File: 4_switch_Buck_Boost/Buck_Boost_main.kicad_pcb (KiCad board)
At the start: 4 copper layers, 95 parts, among them J1 Conn_02x02_Counter_Clockwise, J2 Screw_Terminal_2x5.08, J3 Screw_Terminal_2x2.54, J4 Screw_Terminal_2x5.08, Q1 CSD18532Q5B, Q101 2N7002K, Q102 NVMFS6H836NLT1G, Q103 BSS83P, Q2 CSD18532Q5B, Q3 CSD18532Q5B, Q4 CSD18532Q5B, U1 LT8390EUFD_PBF, U101 LTC4372CMS8-PBF

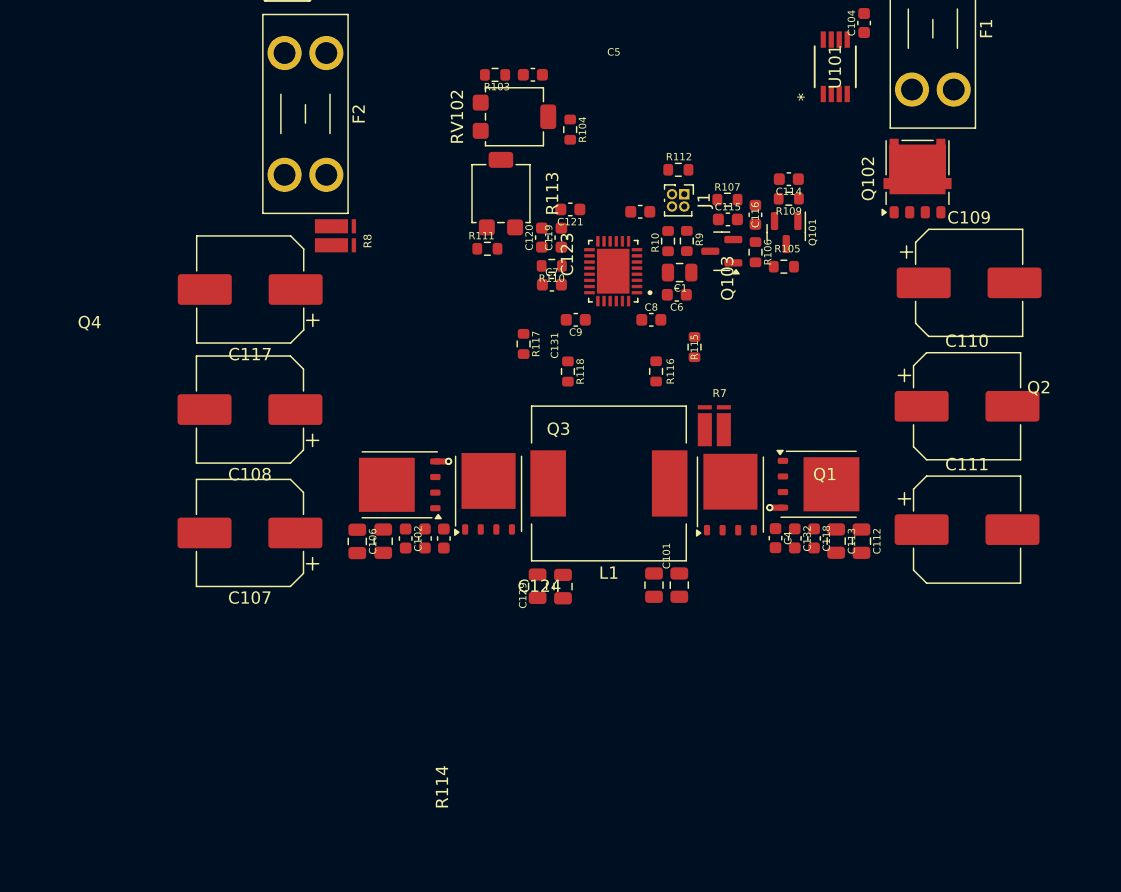
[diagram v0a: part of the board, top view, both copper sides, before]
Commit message: Latest FET and Inductor update, Connected Analog traces
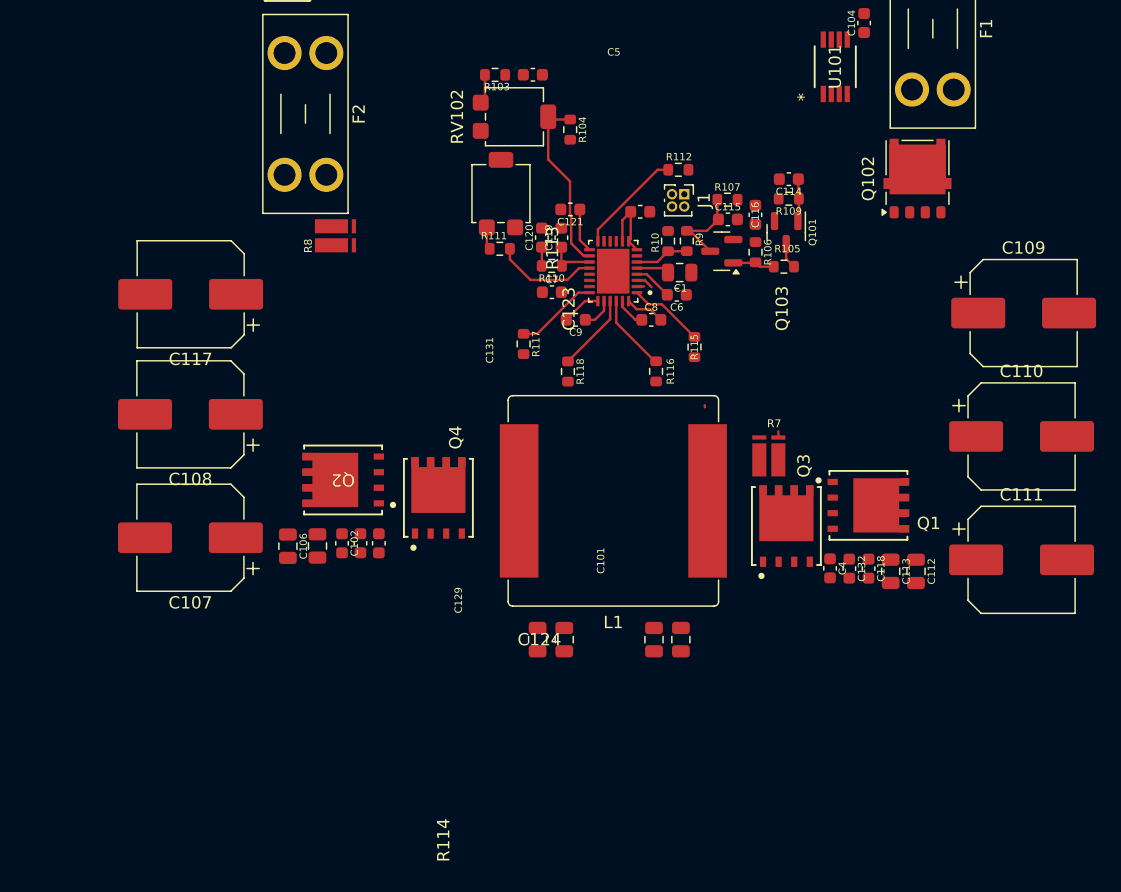
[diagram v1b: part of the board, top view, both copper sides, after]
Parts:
- L1: footprint Inductor_SMD:L_Wuerth_WE-PD-Typ-LS -> Inductor_SMD:L_Bourns_SRP1770TA_16.9x16.9mm
- Q1, Q2, Q3, Q4: value CSD18532Q5B -> BSC070N10LS5ATMA1; footprint Package_TO_SOT_SMD:TDSON-8-1 -> Infineon BSC070:PG-TDSON-8-7_INF
- moved C106 5.66 mm to (117.7, 124.2)
- moved C101 5.37 mm to (120.2, 124.2)
- moved C131 5.31 mm to (125.2, 124.0)
- moved C129 5.27 mm to (123.7, 124.0)
- moved Q3 5.23 mm to (158.3, 122.5)
- moved C102 5.20 mm to (122.2, 124.0)
- moved C109 5.08 mm to (177.7, 105.2)
- moved C4 5.08 mm to (161.9, 126.0)
- moved C110 5.08 mm to (177.5, 115.2)
- moved C111 5.08 mm to (177.5, 125.3)
- moved C112 5.08 mm to (168.9, 126.2)
- moved C113 5.08 mm to (166.8, 126.2)
- moved C118 5.08 mm to (165.0, 126.0)
- moved C132 5.08 mm to (163.5, 126.0)
- moved R7 5.08 mm to (156.9, 116.8)
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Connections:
- C124 pad 1: SW2 -> Net-(C124-Pad1)
- C124 pad 2: Net-(C124-Pad2) -> SW2
- R113 pad 1: Net-(C123-Pad2) -> GND
- R113 pad 2: GND -> Net-(C123-Pad2)
- R114 pad 1: Net-(C124-Pad2) -> GND
- R114 pad 2: GND -> Net-(C124-Pad1)
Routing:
- net FB: track 0.00 -> 14.9 mm
- net Net-(U1-~{PGOOD}): track 0.00 -> 8.70 mm
- net Net-(U1-RT): track 0.00 -> 8.43 mm
- net Net-(Q103-D): track 0.00 -> 7.20 mm
- net TG2_CTRL: track 0.00 -> 6.75 mm
- net BG2_CTRL: track 0.00 -> 6.33 mm
- net BG1_CTRL: track 0.00 -> 6.30 mm
- net TG1_CTRL: track 0.00 -> 6.18 mm
- net /Vref: track 0.00 -> 6.13 mm
- net EN/UVLO: track 0.00 -> 4.43 mm
- net Net-(U1-VC): track 0.00 -> 3.92 mm
- net Net-(U1-SS): track 0.00 -> 3.61 mm
- net ENABLE: track 0.00 -> 3.47 mm
- net Net-(Q103-G): track 0.00 -> 3.46 mm
- net SW1: track 0.00 -> 3.26 mm
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
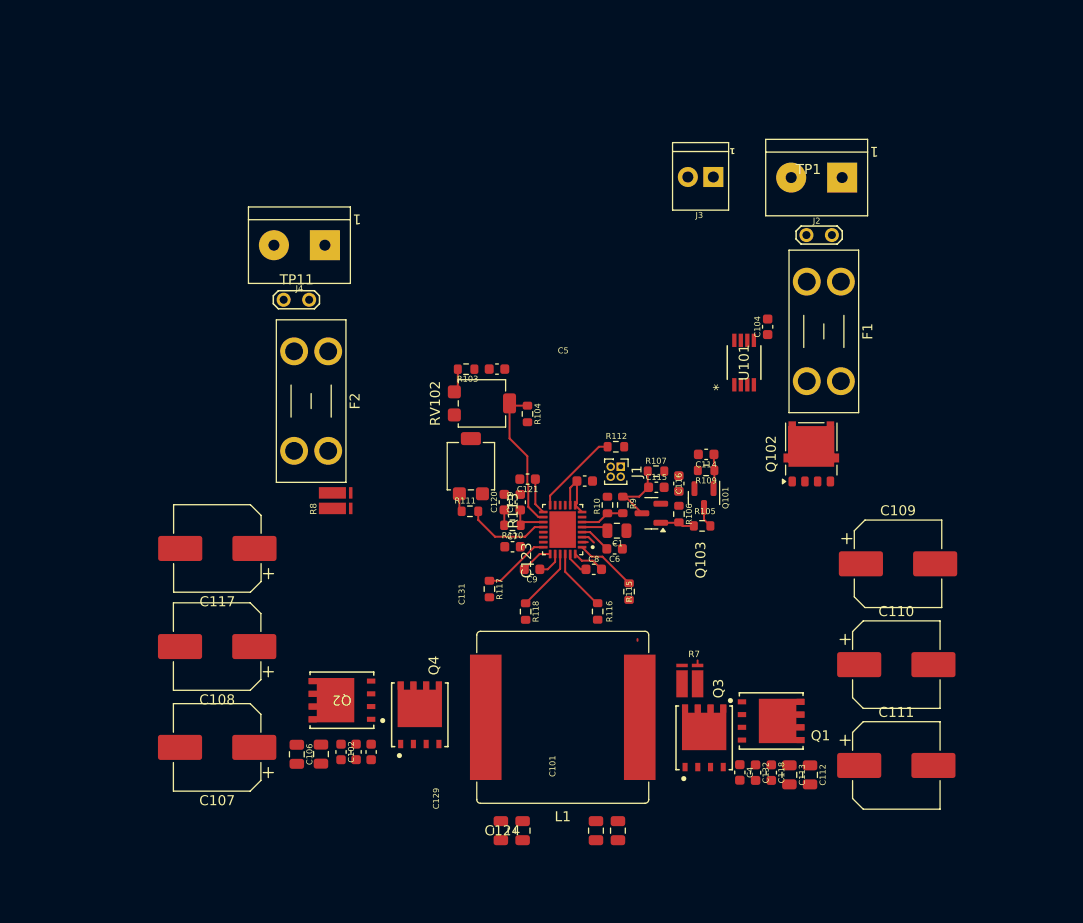
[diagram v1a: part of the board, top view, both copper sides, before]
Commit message: All 4 layers configured
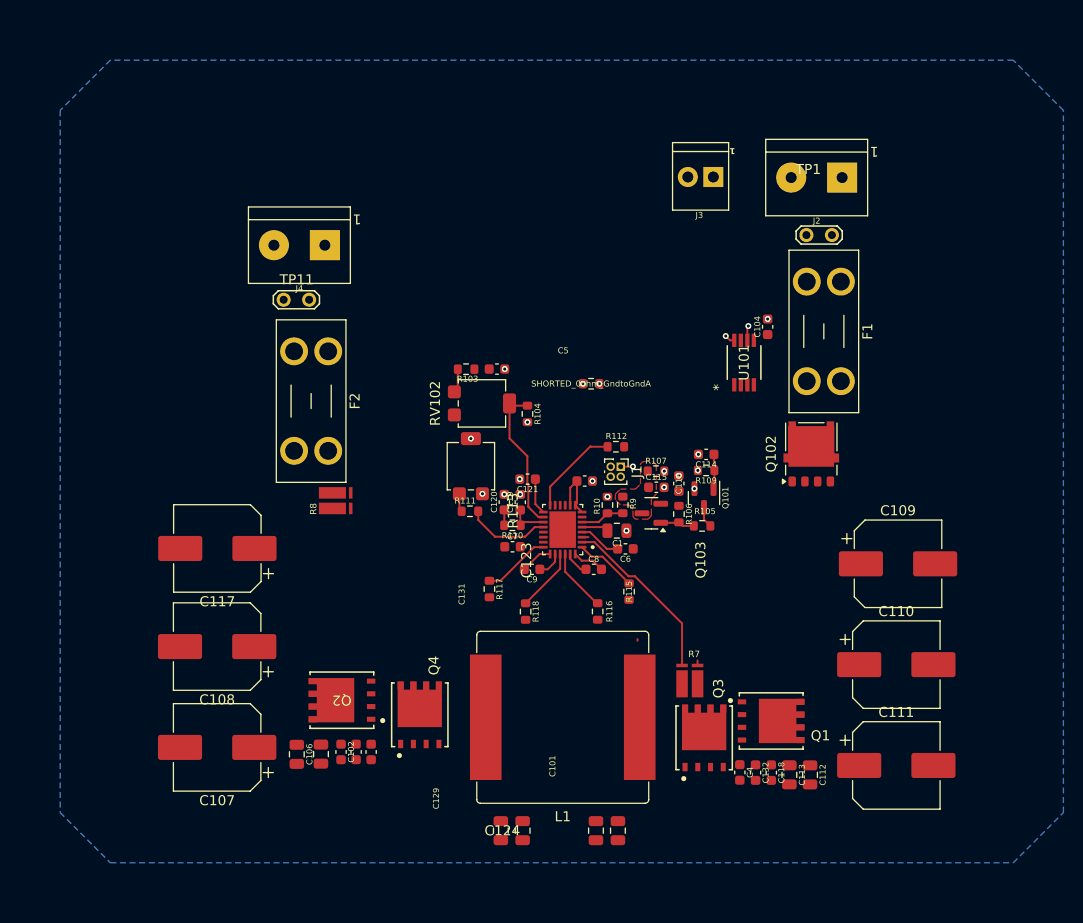
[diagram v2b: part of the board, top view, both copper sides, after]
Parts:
- added SHORTED_0ohm_GndtoGndA: R_short, rsx_resistors:R_0603_1608Metric, F.Cu at (147.1, 87.2)
- moved C6 1.08 mm to (150.5, 103.7)
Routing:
- net LSP: track 0.75 -> 17.7 mm
- net Net-(Q103-D): track 7.20 -> 0.37 mm
- net GND: track 0.00 -> 2.49 mm, vias 0 -> 10
- net GNDA: track 0.00 -> 1.23 mm, vias 0 -> 12
- net Vin: track 3.66 -> 4.74 mm
- net LSN: track 1.92 -> 1.14 mm
- net Net-(U1-~{PGOOD}): track 8.70 -> 9.25 mm
- added copper zone on B.Cu, net GND
- added copper zone on In1.Cu, net GND
- added copper zone on In1.Cu, net GNDA
- added copper zone on F.Cu, net Net-(Q103-D)
- added copper zone on In2.Cu, net Vin

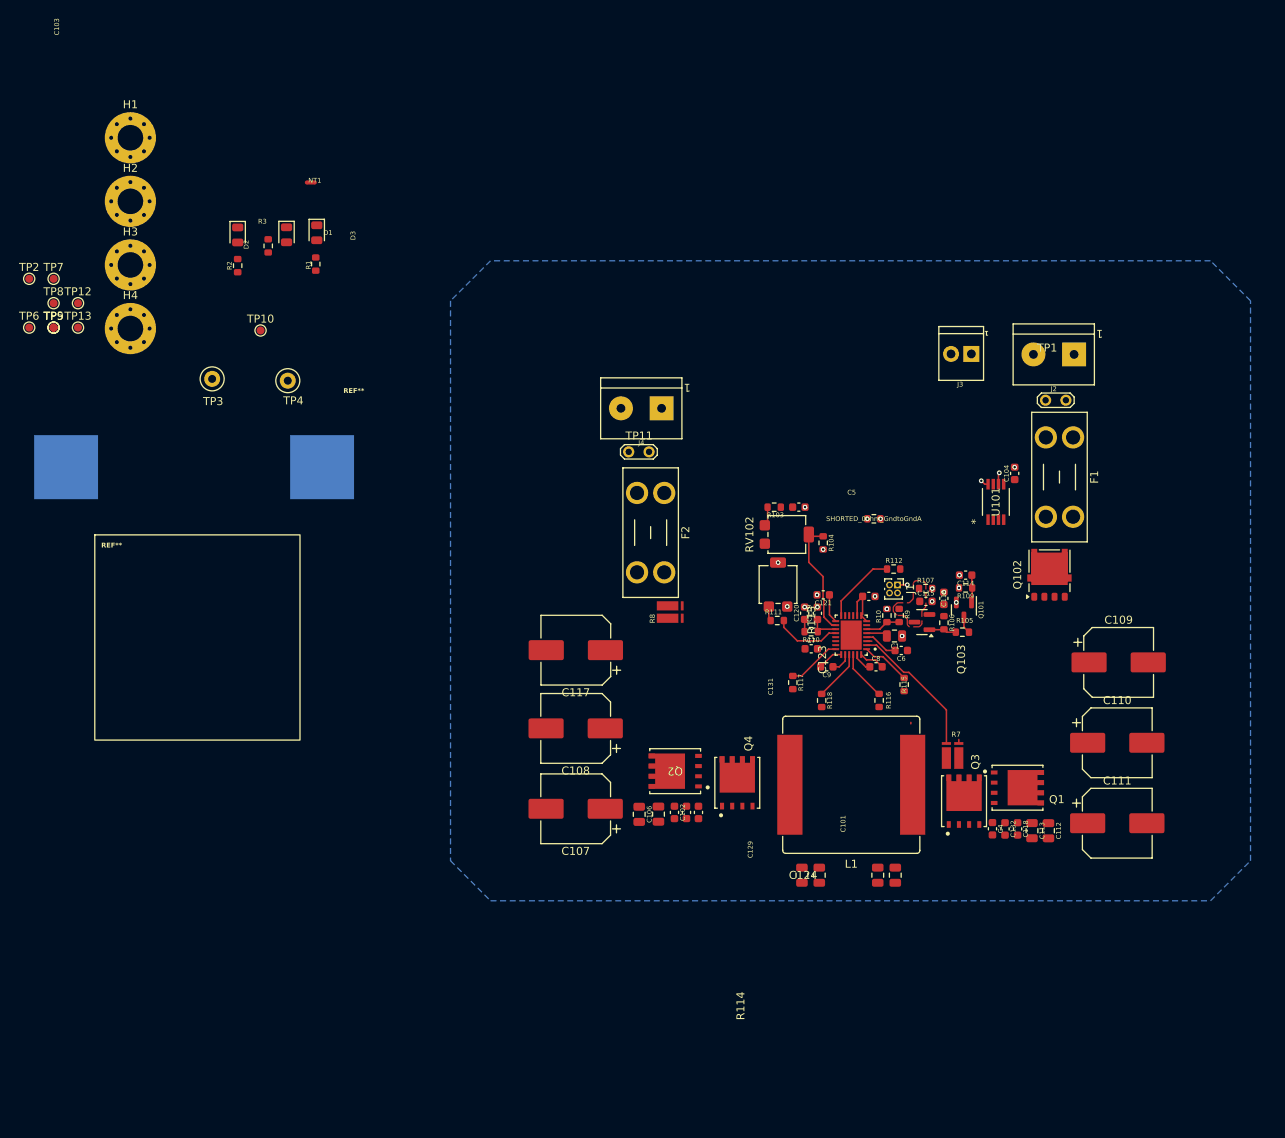
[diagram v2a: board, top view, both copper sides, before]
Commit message: Rsense footprint changes
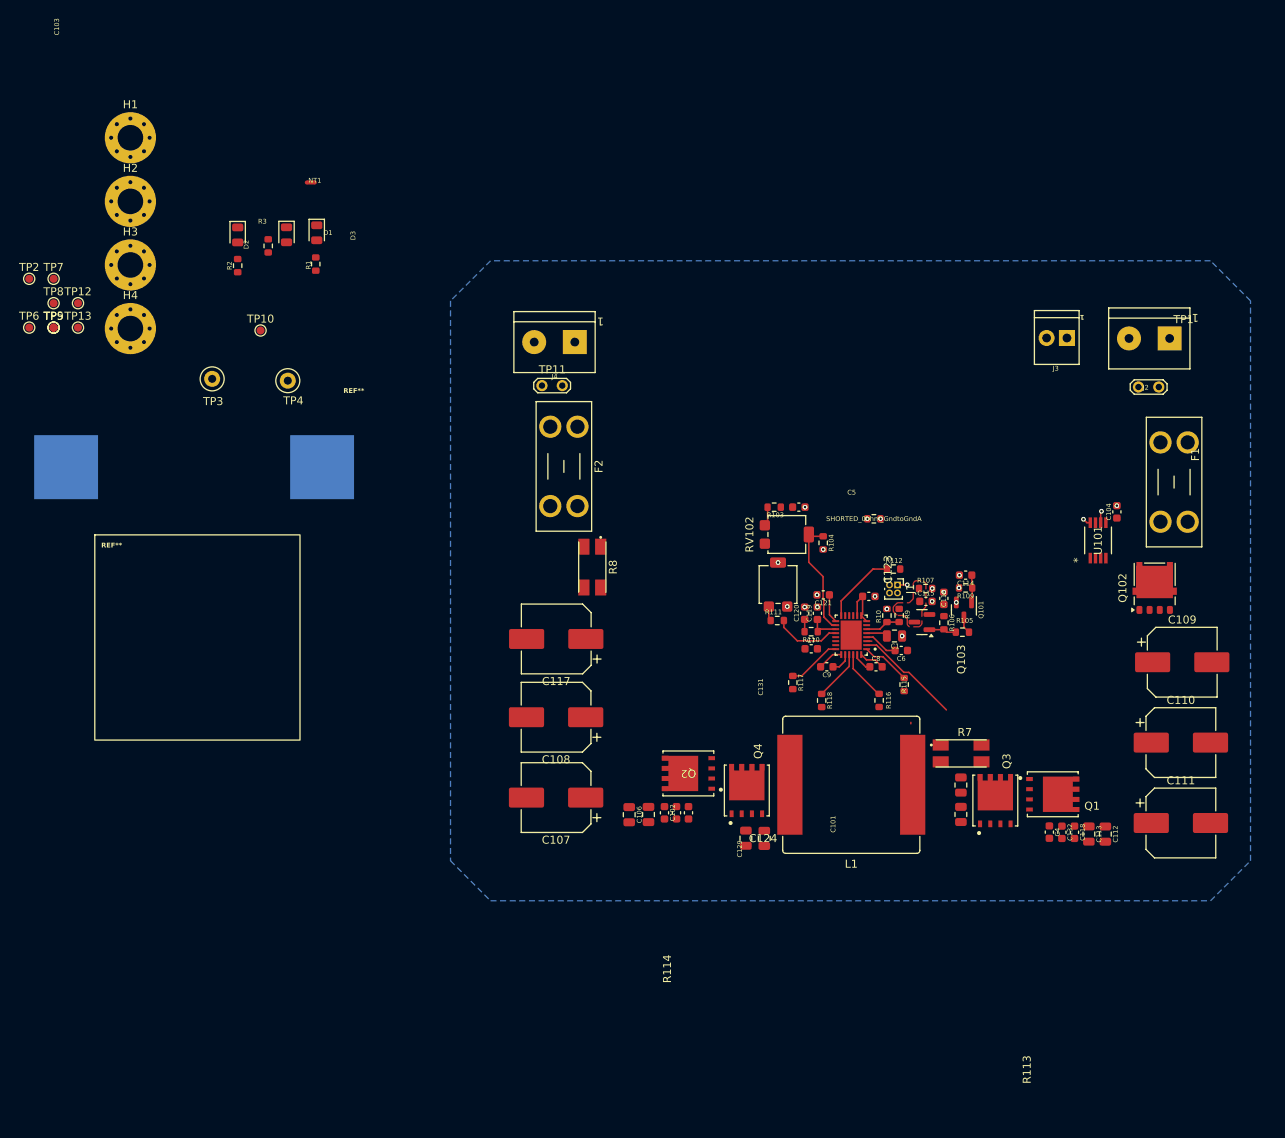
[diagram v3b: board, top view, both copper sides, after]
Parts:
- R7, R8: footprint shunt:RES_KRL3216T4-M-R003-F-T1 -> Rsense_Littelfuse_L4CL:R_2512_4Pad_Littelfuse_L4CL
- moved F1 14.3 mm to (186.3, 77.7)
- moved C123 13.9 mm to (158.0, 120.5)
- moved U101 13.7 mm to (175.1, 90.0)
- moved C104 13.7 mm to (177.5, 86.4)
- moved J4 13.6 mm to (109.7, 65.2)
- moved TP11 13.6 mm to (105.6, 70.6)
- moved F2 13.6 mm to (110.0, 75.7)
- moved Q102 13.3 mm to (182.2, 95.9)
- moved R113 12.9 mm to (158.0, 124.2), turned to 90 degrees
- moved J3 12.1 mm to (170.4, 64.6)
- moved J2 12.1 mm to (184.0, 64.7)
- moved TP1 11.7 mm to (180.2, 70.8)
- moved R8 11.2 mm to (111.9, 93.3)
- moved R114 10.3 mm to (131.1, 127.2)
- moved C109 7.95 mm to (185.6, 105.2)
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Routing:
- net LSP: track 17.7 -> 13.5 mm
- net LSN: track 1.14 -> 0.64 mm

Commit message: correct resistor footprint
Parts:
- R7: footprint Rsense_Littelfuse_L4CL:R_2512_4Pad_Littelfuse_L4CL -> Littelfuse_L4CA0612_KiCad9:Littelfuse_L4CA0612_4Terminal
- moved C123 8.71 mm to (156.6, 129.1)
- moved R113 4.58 mm to (159.4, 128.6)
- moved R7 2.92 mm to (155.5, 118.2)
- moved Q1 2.47 mm to (167.2, 120.7)
- moved Q3 2.33 mm to (160.2, 121.3)
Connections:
- R7 pad 1: LSP -> LSN
- R7 pad 4: LSN -> LSP

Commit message: MOSFET footprint and symbol update
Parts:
- removed Q1, Q2, Q3, Q4: BSC070N10LS5ATMA1, Infineon BSC070:PG-TDSON-8-7_INF
- added Q104: BSC070N10LS5, RSX_TDSON:TDSON-8-1, F.Cu at (169.5, 120.7)
- added Q105: BSC070N10LS5, RSX_TDSON:TDSON-8-1, F.Cu at (125.0, 119.0)
- added Q106: BSC070N10LS5, RSX_TDSON:TDSON-8-1, F.Cu at (131.7, 119.4)
- added Q107: BSC070N10LS5, RSX_TDSON:TDSON-8-1, F.Cu at (161.3, 121.4)
- R8: footprint Rsense_Littelfuse_L4CL:R_2512_4Pad_Littelfuse_L4CL -> Littelfuse_L4CA0612_KiCad9:Littelfuse_L4CA0612_4Terminal

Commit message: Input power loop pores
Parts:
- moved TP8 129.8 mm to (167.8, 101.0)
- moved TP3 108.6 mm to (163.6, 113.9)
- moved R1 99.7 mm to (169.0, 94.5)
- moved D1 99.6 mm to (169.0, 90.7)
- moved R3 92.7 mm to (157.8, 86.6)
- moved D3 92.7 mm to (160.1, 85.2)
- moved C123 7.05 mm to (156.5, 122.1)
- moved TP1 7.00 mm to (187.2, 70.9), turned to 180 degrees
- moved R116 5.22 mm to (152.9, 109.4), turned to 0 degrees
- moved R113 3.91 mm to (156.6, 125.8)
- moved C111 3.85 mm to (185.3, 121.4)
- moved C109 3.85 mm to (185.5, 101.3)
- moved C110 3.85 mm to (185.3, 111.4)
- moved C1 3.59 mm to (152.8, 103.7), turned to 90 degrees
- moved Q102 3.25 mm to (183.1, 92.8)
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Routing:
- net Net-(Q104-G): track 0.00 -> 19.5 mm, vias 0 -> 2
- net Net-(Q107-G): track 0.00 -> 18.2 mm, vias 0 -> 2
- net LSN: track 0.64 -> 16.8 mm, vias 0 -> 2
- net Net-(Q102-G): track 0.00 -> 12.2 mm, vias 0 -> 2
- net BG1_CTRL: track 6.30 -> 11.6 mm
- net Vin: track 4.74 -> 0.49 mm
- net LSP: track 13.5 -> 16.5 mm, vias 0 -> 2
- net /INTVCC: track 2.67 -> 0.00 mm
- net TG1_CTRL: track 6.18 -> 7.43 mm
- net SW1: track 3.26 -> 2.33 mm
- net Net-(U1-BST1): track 2.48 -> 1.89 mm
- net Net-(Q103-G): track 3.46 -> 3.96 mm
- net GNDA: vias 12 -> 11
- added copper zone on F.Cu, net Net-(L1-Pad1)
- added copper zone on F.Cu, net SW1
- added copper zone on F.Cu, net Vin

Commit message: Updated Pores
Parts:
- moved F3 6.17 mm to (68.2, 80.2)
- moved TP11 2.81 mm to (108.2, 71.5)
- moved J4 2.37 mm to (112.0, 65.5)
- moved F2 1.42 mm to (111.2, 76.5)
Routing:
- net Net-(Q102-D): track 0.00 -> 15.7 mm
- net FB: track 14.9 -> 20.9 mm
- net Net-(C124-Pad1): track 0.00 -> 2.31 mm
- net Net-(C123-Pad2): track 0.00 -> 1.90 mm
- net SW2: vias 0 -> 22
- net GNDA: vias 11 -> 12
- net GND: vias 10 -> 88
- added copper zone on F.Cu, net GND
- added copper zone on B.Cu, net SW2
- added copper zone on F.Cu, net SW2
- added copper zone on In2.Cu, net SW2
- added copper zone on F.Cu, net Vout
